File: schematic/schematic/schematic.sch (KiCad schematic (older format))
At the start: 17 parts

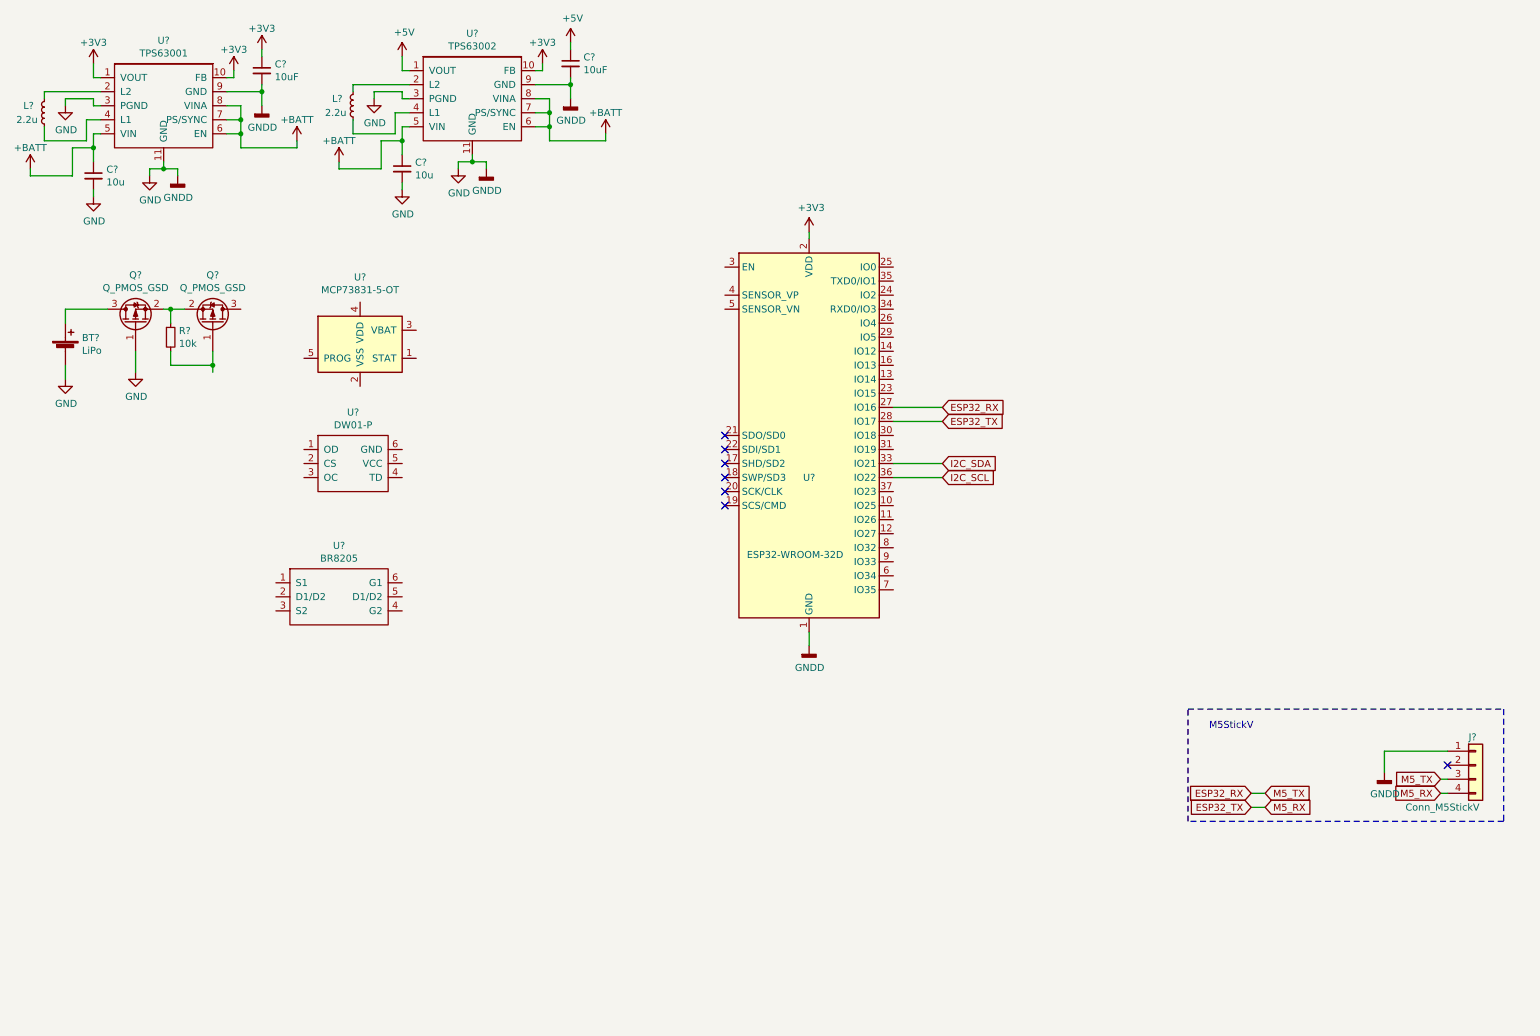
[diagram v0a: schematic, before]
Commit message: drawing schematic(still remain servo)
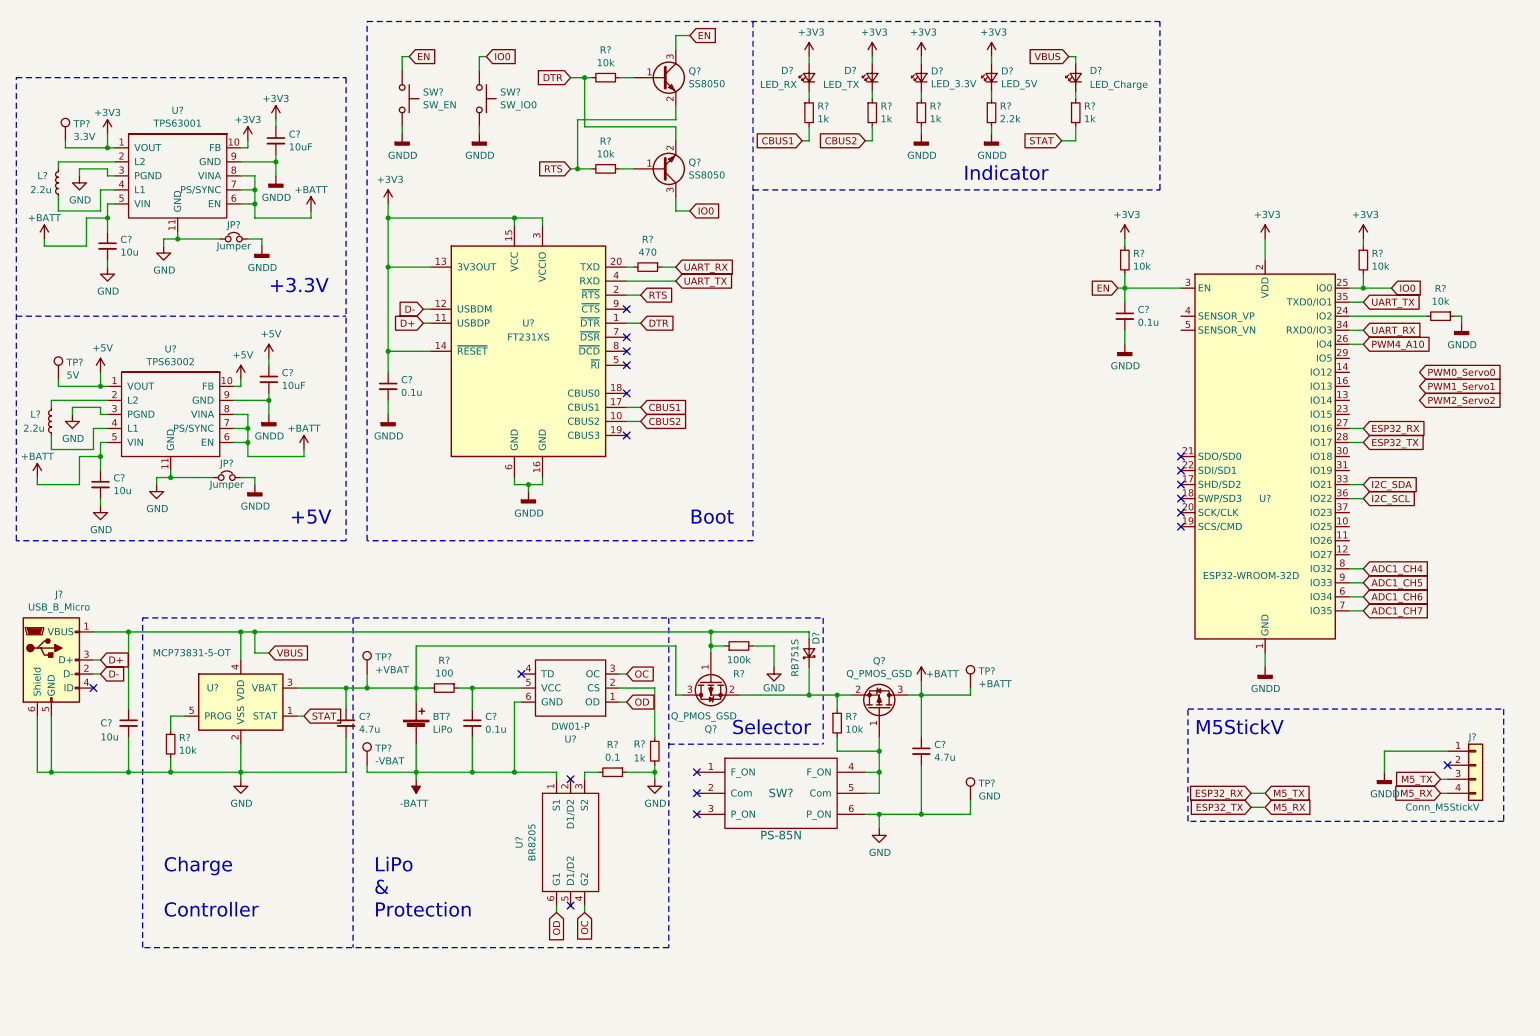
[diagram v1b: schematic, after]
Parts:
- removed Q?: Q_PMOS_GSD, symbol Device:Q_PMOS_GSD
- added C? (x3): 0.1u, symbol Device:C_Small
- added C?: 10u, symbol Device:C_Small
- added C? (x2): 4.7u, symbol Device:C_Small
- added D?: LED_Charge, symbol Device:LED_Small
- added D?: RB751S, symbol Device:D_Schottky_Small
- added D?: LED_RX, symbol Device:LED_Small
- added D?: LED_TX, symbol Device:LED_Small
- added D?: LED_3.3V, symbol Device:LED_Small
- added D?: LED_5V, symbol Device:LED_Small
- added J?: USB_B_Micro, symbol Connector:USB_B_Micro
- added JP? (x2): Jumper, symbol Device:Jumper_NC_Small
- added Q?: Q_PMOS_GSD, symbol Device:Q_PMOS_GSD
- added Q? (x2): SS8050, symbol Device:Q_NPN_BEC
- added R? (x6): 10k, symbol Device:R_Small
- added R? (x5): 1k, symbol Device:R_Small
- added R?: 100k, symbol Device:R_Small
- added R?: 100, symbol Device:R_Small
- added R?: 0.1, symbol Device:R_Small
- added R?: 470, symbol Device:R_Small
- added R?: 2.2k, symbol Device:R_Small
- added SW?: SW_EN, symbol Switch:SW_Push
- added SW?: SW_IO0, symbol Switch:SW_Push
- added SW?: PS-85N, symbol micelib:PS-85N
- added TP?: +VBAT, symbol Connector:TestPoint
- added TP?: -VBAT, symbol Connector:TestPoint
- added TP?: +BATT, symbol Connector:TestPoint
- added TP?: GND, symbol Connector:TestPoint
- added TP?: 5V, symbol Connector:TestPoint
- added TP?: 3.3V, symbol Connector:TestPoint
- added U?: FT231XS, Package_SO:SSOP-20_3.9x8.7mm_P0.635mm, symbol Interface_USB:FT231XS
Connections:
- net +3V3: now also C?.1, D?.2 (A), D?.2 (A), D?.2 (A), D?.2 (A), R?.1, R?.1, TP?.1, U?.13 (3V3OUT), U?.14 (~RESET), U?.15 (VCC), U?.3 (VCCIO); no longer U?.10 (FB)
- net +5V: now also U?.10 (FB), TP?.1
- net +BATT: now also Q?.3 (D), C?.1, TP?.1
- net GND: now also U?.2 (VSS), C?.2, C?.2, C?.2, J?.5 (GND), J?.6 (Shield), JP?.1, JP?.1, R?.1, R?.2, R?.2, R?.2, SW?.6 (P_ON), TP?.1; no longer BT?.2 (-), C?.2, C?.2, J?.1 (Pin_1), U?.1 (GND), U?.15 (GND), U?.38 (GND), U?.9 (GND), U?.9 (GND)
- net at U?.24 (IO2): now also R?.2
- net IO0: now reaches U?.25 (IO0)
- net IO0: now also Q?.3 (C), R?.2, SW?.1
- net PWM4_A10: now reaches U?.26 (IO4)
- net EN: now reaches U?.3 (EN)
- net EN: now also C?.1, Q?.3 (C), R?.2, SW?.1
- net UART_RX: now reaches U?.34 (RXD0/IO3)
- net UART_RX: now also R?.1
- net UART_TX: now reaches U?.35 (TXD0/IO1)
- net UART_TX: now also U?.4 (RXD)
- net ADC1_CH6: now reaches U?.6 (IO34)
- net ADC1_CH7: now reaches U?.7 (IO35)
- net ADC1_CH4: now reaches U?.8 (IO32)
- net ADC1_CH5: now reaches U?.9 (IO33)
- net at BT?.1 (+): now also U?.3 (VBAT), C?.1, Q?.3 (D), R?.2, TP?.1
- net at Q?.2 (S), R?.1: now also D?.1 (K), Q?.2 (S)
- net at Q?.1 (G), R?.2: now also SW?.4 (F_ON), SW?.5 (Com)
- net STAT: now reaches U?.1 (STAT)
- net STAT: now also R?.2
- net VBUS: now reaches U?.4 (VDD)
- net VBUS: now also C?.1, D?.2 (A), D?.2 (A), J?.1 (VBUS), Q?.1 (G), R?.1
- net at U?.5 (PROG): now also R?.1
- net OD: now reaches U?.1 (OD)
- net OD: now also U?.6 (G1)
- net at U?.2 (CS): now also R?.1
- net OC: now reaches U?.3 (OC)
- net OC: now also U?.4 (G2)
- net at U?.5 (VCC): now also C?.1, R?.1
- net -BATT: now reaches U?.6 (GND)
- net -BATT: now also BT?.2 (-), U?.1 (S1), C?.2, TP?.1
- net at U?.3 (S2): now also R?.2
- new net: D?.1 (K), R?.1 (x5)
- new net: Q?.1 (B), R?.1 (x2)
- new net: R?.2, U?.20 (TXD)
- new net CBUS1: R?.2, U?.17 (CBUS1)
- new net CBUS2: R?.2, U?.10 (CBUS2)
- new net D+: J?.3 (D+), U?.11 (USBDP)
- new net D-: J?.2 (D-), U?.12 (USBDM)
- new net DTR: Q?.2 (E), R?.2, U?.1 (~DTR)
- new net GNDD: C?.2, C?.2, C?.2, C?.2, J?.1 (Pin_1), JP?.2, JP?.2, R?.1, R?.2, R?.2, SW?.2, SW?.2, U?.1 (GND), U?.15 (GND), U?.16 (GND), U?.38 (GND), U?.6 (GND), U?.9 (GND), U?.9 (GND)
- new net RTS: Q?.2 (E), R?.2, U?.2 (~RTS)
- no-connect marks 7 -> 20
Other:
- note added: "+3.3V"
- note added: "+5V"
- note added: "Boot"
- note added: "Charge\n\nController"
- note added: "Indicator"
- note added: "LiPo\n&\nProtection"
- note added: "Selector"
- moved on the sheet: BT?, C?, L?, Q?, R?, U?

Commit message: Drawing Circuit (Add some indicators)
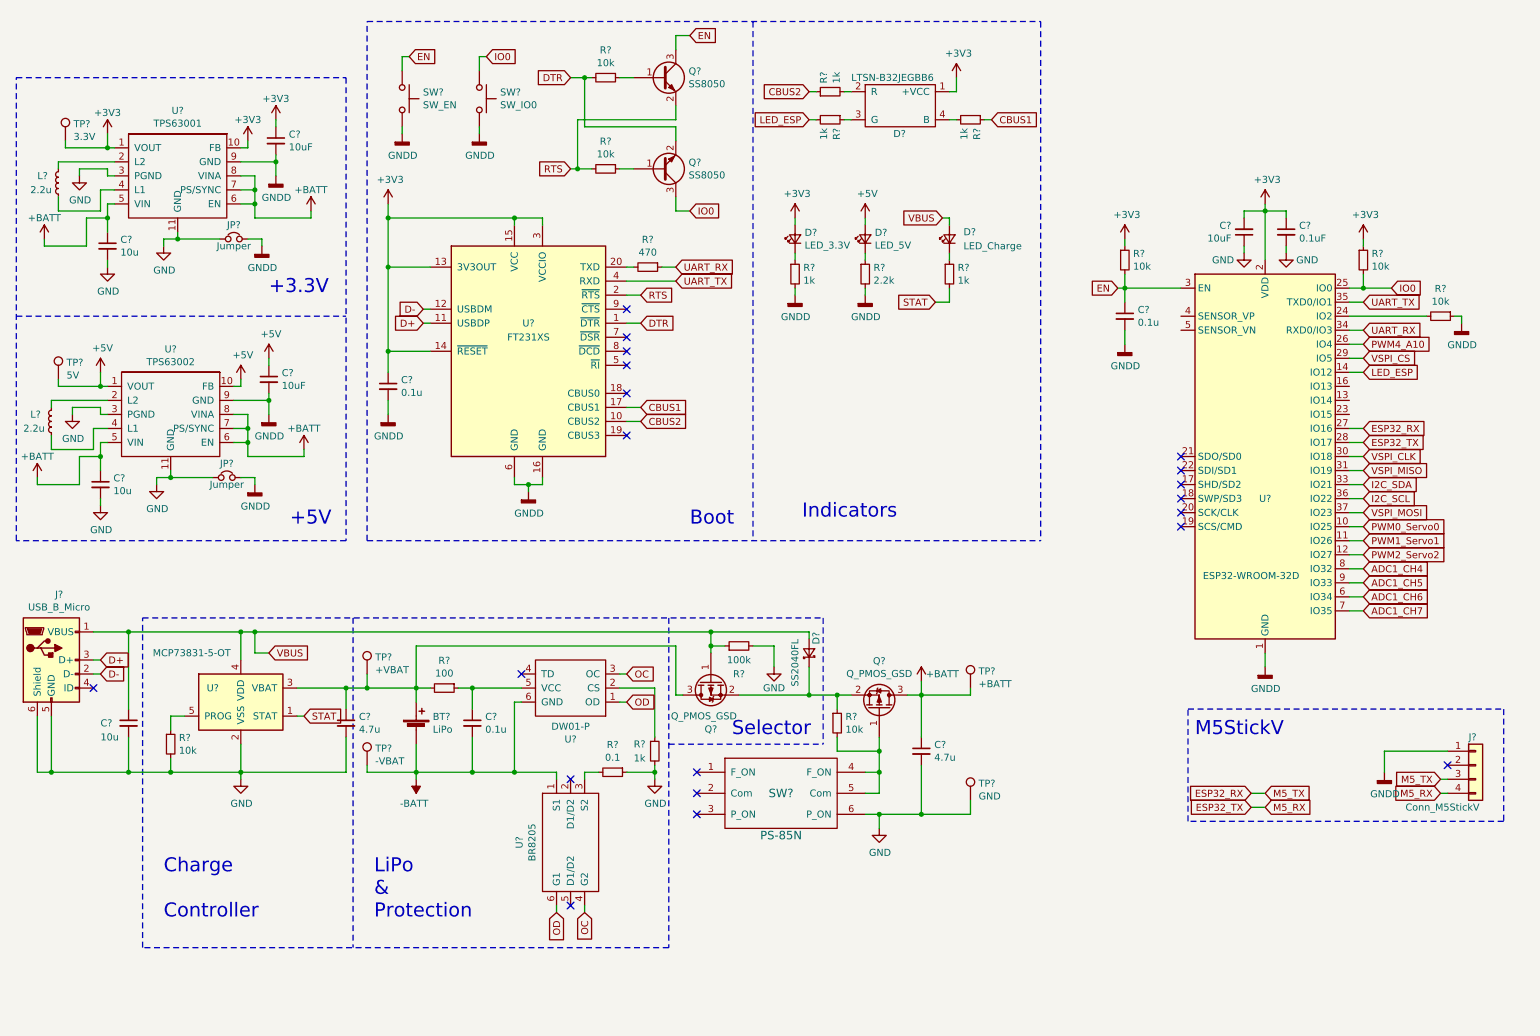
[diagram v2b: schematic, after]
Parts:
- removed D?: LED_RX, symbol Device:LED_Small
- removed D?: LED_TX, symbol Device:LED_Small
- added C?: 0.1uF, symbol Device:C_Small
- added C?: 10uF, symbol Device:C_Small
- added D?: LTSN-B32JEGBB6, symbol micelib:LTSN-B32JEGBB6
- added R?: 1k, symbol Device:R_Small
- D?: value RB751S -> SS2040FL
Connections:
- net +3V3: now also C?.1, C?.2, D?.1 (+VCC); no longer D?.2 (A)
- net +5V: now also D?.2 (A)
- net CBUS1: now also R?.1; no longer R?.2
- net CBUS2: now also R?.1; no longer R?.2
- net GND: now also C?.1, C?.2
- net PWM0_Servo0: now also U?.10 (IO25)
- net PWM1_Servo1: now also U?.11 (IO26)
- net PWM2_Servo2: now also U?.12 (IO27)
- net LED_ESP: now reaches U?.14 (IO12)
- net LED_ESP: now also R?.2
- net VSPI_CS: now reaches U?.29 (IO5)
- net VSPI_CLK: now reaches U?.30 (IO18)
- net VSPI_MISO: now reaches U?.31 (IO19)
- net VSPI_MOSI: now reaches U?.37 (IO23)
- new net: D?.2 (R), R?.2
- new net: D?.3 (G), R?.1
- new net: D?.4 (B), R?.2
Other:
- note added: "Indicators"
- note removed: "Indicator"
- moved on the sheet: D?, R?

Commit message: 回路書き終わった．
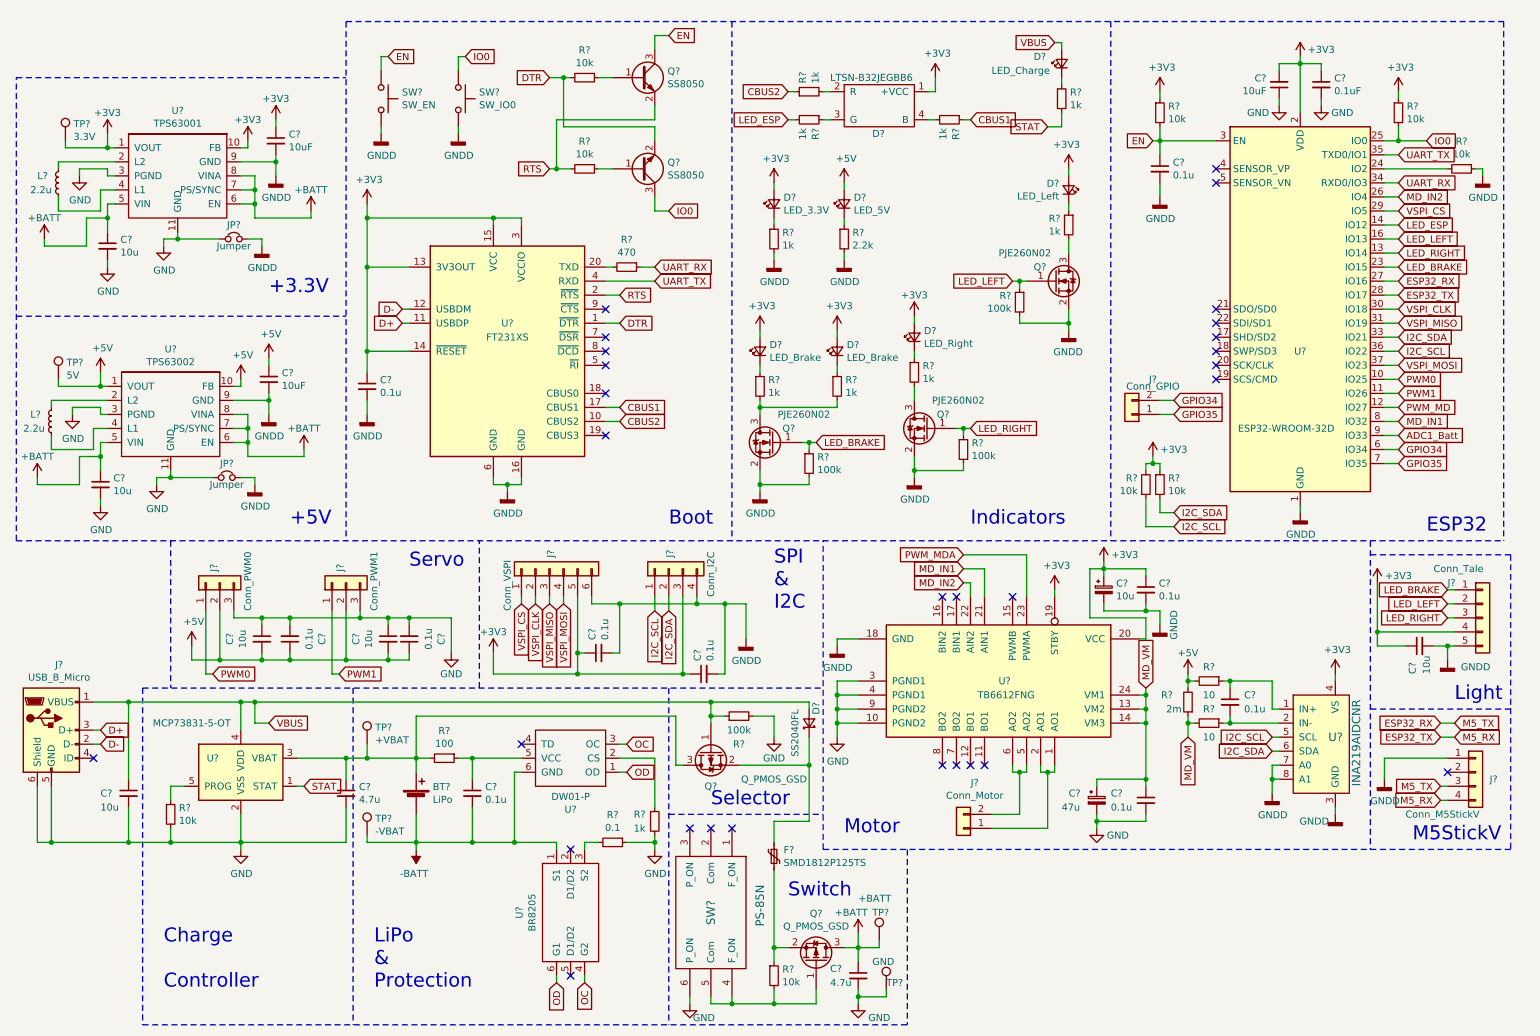
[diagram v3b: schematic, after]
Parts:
- added C? (x7): 0.1u, symbol Device:C_Small
- added C? (x3): 10u, symbol Device:C_Small
- added C?: 47u, symbol Device:CP_Small
- added C?: 10u, symbol Device:CP_Small
- added D? (x2): LED_Brake, symbol Device:LED_Small
- added D?: LED_Right, symbol Device:LED_Small
- added D?: LED_Left, symbol Device:LED_Small
- added F?: SMD1812P125TS, symbol Device:Polyfuse_Small
- added J?: Conn_I2C, symbol Connector_Generic:Conn_01x04
- added J?: Conn_VSPI, symbol Connector_Generic:Conn_01x06
- added J?: Conn_PWM0, symbol Connector_Generic:Conn_01x03
- added J?: Conn_PWM1, symbol Connector_Generic:Conn_01x03
- added J?: Conn_Tale, symbol Connector_Generic:Conn_01x05
- added J?: Conn_Motor, symbol Connector_Generic:Conn_01x02
- added J?: Conn_GPIO, symbol Connector_Generic:Conn_01x02
- added Q? (x3): PJE260N02, symbol Device:Q_NMOS_GSD
- added R? (x4): 1k, symbol Device:R_Small
- added R? (x3): 100k, symbol Device:R_Small
- added R? (x2): 10k, symbol Device:R_Small
- added R? (x2): 10, symbol Device:R_Small
- added R?: 2m, symbol Device:R_Small
- added U?: TB6612FNG, Package_SO:SSOP-24_5.3x8.2mm_P0.65mm, symbol Driver_Motor:TB6612FNG
- added U?: INA219AIDCNR, digikey-footprints:SOT-23-8, symbol dk_PMIC-Current-Regulation-Management:INA219AIDCNR
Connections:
- net +3V3: now also C?.1, C?.1, C?.1, C?.1, C?.1, D?.2 (A), D?.2 (A), D?.2 (A), D?.2 (A), J?.3 (Pin_3), J?.4 (Pin_4), J?.5 (Pin_5), R?.1, R?.2, U?.19 (STBY), U?.20 (VCC), U?.4 (VS)
- net +5V: now also C?.1, C?.1, C?.2, C?.2, J?.2 (Pin_2), J?.2 (Pin_2), R?.2, R?.2
- net GND: now also C?.1, C?.1, C?.2, C?.2, C?.2, C?.2, J?.3 (Pin_3), J?.3 (Pin_3), U?.10 (PGND2), U?.3 (PGND1), U?.4 (PGND1), U?.9 (PGND2)
- net GNDD: now also C?.2, C?.2, C?.2, C?.2, C?.2, J?.4 (Pin_4), J?.5 (Pin_5), J?.6 (Pin_6), Q?.2 (S), Q?.2 (S), Q?.2 (S), R?.2, R?.2, R?.2, U?.18 (GND), U?.3 (GND), U?.7 (A0), U?.8 (A1)
- net I2C_SCL: now also J?.1 (Pin_1), R?.1, U?.5 (SCL)
- net I2C_SDA: now also J?.2 (Pin_2), R?.2, U?.6 (SDA)
- net VSPI_CLK: now also J?.2 (Pin_2)
- net VSPI_CS: now also J?.1 (Pin_1)
- net VSPI_MISO: now also J?.3 (Pin_3)
- net VSPI_MOSI: now also J?.4 (Pin_4)
- net LED_RIGHT: now reaches U?.13 (IO14)
- net LED_RIGHT: now also J?.3 (Pin_3), Q?.1 (G), R?.1
- net LED_LEFT: now reaches U?.16 (IO13)
- net LED_LEFT: now also J?.2 (Pin_2), Q?.1 (G), R?.1
- net LED_BRAKE: now reaches U?.23 (IO15)
- net LED_BRAKE: now also J?.1 (Pin_1), Q?.1 (G), R?.1
- net at D?.1 (K), Q?.2 (S): now also F?.1; no longer Q?.2 (S), R?.1
- net ADC1_CH4 renamed MD_IN1
- net MD_IN1: now also U?.21 (AIN1)
- net ADC1_CH5 renamed ADC1_Batt
- net ADC1_CH6 renamed GPIO34
- net GPIO34: now also J?.2 (Pin_2)
- net ADC1_CH7 renamed GPIO35
- net GPIO35: now also J?.1 (Pin_1)
- net PWM0_Servo0 renamed PWM0
- net PWM0: now also J?.1 (Pin_1)
- net PWM1_Servo1 renamed PWM1
- net PWM1: now also J?.1 (Pin_1)
- net PWM2_Servo2 renamed PWM_MD
- net PWM4_A10 renamed MD_IN2
- net MD_IN2: now also U?.22 (AIN2)
- new net: F?.2, Q?.2 (S), R?.1
- new net: D?.1 (K), R?.1 (x4)
- new net: Q?.3 (D), R?.2, R?.2
- new net: Q?.3 (D), R?.2 (x2)
- new net: J?.1 (Pin_1), U?.1 (AO1), U?.2 (AO1)
- new net: J?.2 (Pin_2), U?.5 (AO2), U?.6 (AO2)
- new net: C?.1, R?.1, U?.1 (IN+)
- new net: C?.2, R?.1, U?.2 (IN-)
- new net MD_VM: C?.1, C?.1, R?.1, R?.2, U?.13 (VM2), U?.14 (VM3), U?.24 (VM1)
- new net PWM_MDA: U?.23 (PWMA)
- no-connect marks 20 -> 29
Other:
- note added: "ESP32"
- note added: "Light"
- note added: "Motor"
- note added: "SPI\n&\nI2C"
- note added: "Servo"
- note added: "Switch"
- moved on the sheet: BT?, C?, D?, J?, Q?, R?, SW?, TP?, U?
